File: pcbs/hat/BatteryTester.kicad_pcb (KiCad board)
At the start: 4 copper layers, 162 parts, among them J1 Supply Connector, J2 Battery Connector, J3 Battery Connector, J4 Battery Connector, J5 Battery Connector, J6 Battery Connector, J7 Battery Connector, J8 Battery Connector, J9 Battery Connector, Q1 DMT6009LCT, Q10 AO3414, Q11 DMT6009LCT, Q12 AO3414, Q13 DMT6009LCT, Q14 AO3414, Q15 DMT6009LCT, Q16 AO3414, Q2 AO3414, Q3 DMT6009LCT, Q4 AO3414, Q5 DMT6009LCT, Q6 AO3414, Q7 DMT6009LCT, Q8 AO3414, Q9 DMT6009LCT, U1 INA181A2IDBVR, U10 TP5000_Breakout_Akaddy, U11 INA181A2IDBVR, U12 TP5000_Breakout_Akaddy, U13 INA181A2IDBVR, U14 TP5000_Breakout_Akaddy, U15 INA181A2IDBVR, U16 TP5000_Breakout_Akaddy, U17 NUCLEO-F401RE, U18 ADS7828, U19 ADS7828, U2 TP5000_Breakout_Akaddy, U20 ADS7828, U21 AP2138N-2.5TRG1, U22 LM3480-5.0, U23 SST25VF016B, U3 INA181A2IDBVR, U4 TP5000_Breakout_Akaddy, U5 INA181A2IDBVR, U6 TP5000_Breakout_Akaddy, U7 INA181A2IDBVR, U8 TP5000_Breakout_Akaddy, U9 INA181A2IDBVR

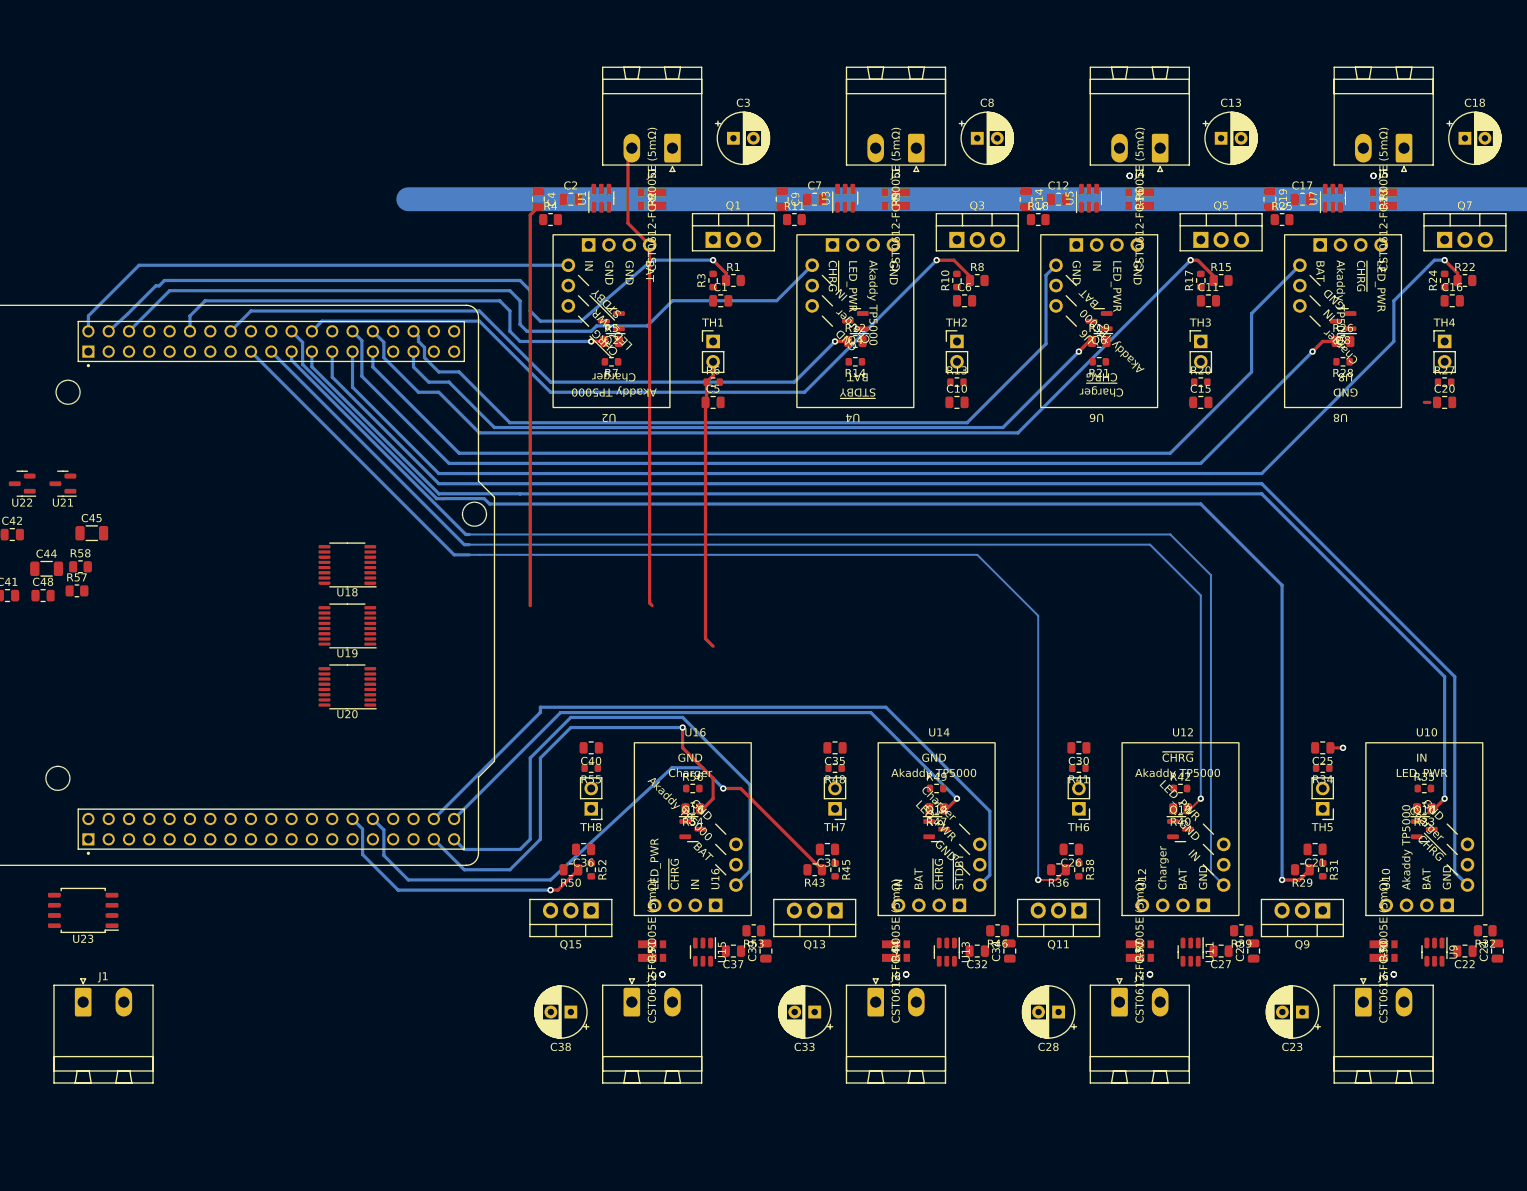
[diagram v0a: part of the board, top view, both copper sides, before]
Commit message: reassign adc's
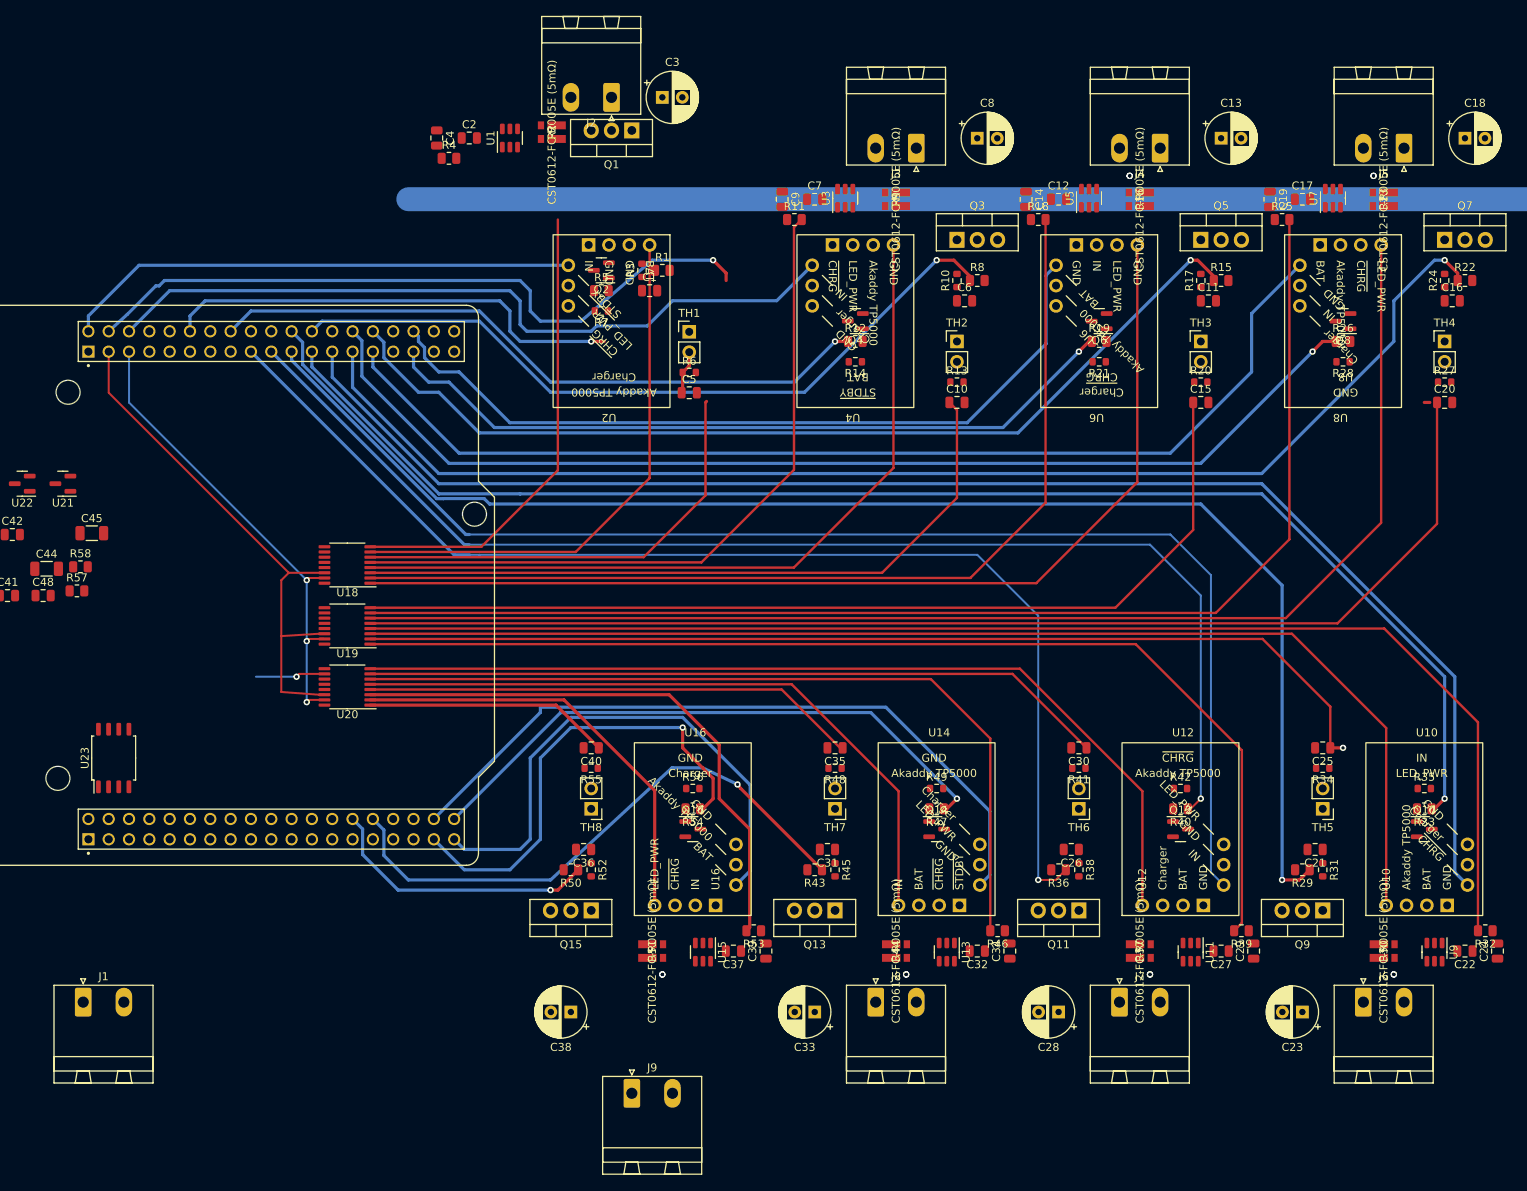
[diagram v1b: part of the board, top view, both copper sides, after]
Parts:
- moved U23 19.4 mm to (336.6, -3.81), turned to 90 degrees
- moved Q1 17.0 mm to (401.3, -82.3), turned to 180 degrees
- moved R2 15.1 mm to (391.3, -82.0)
- moved C4 14.8 mm to (376.9, -81.3)
- moved R4 14.8 mm to (378.5, -78.8)
- moved C2 14.8 mm to (381.0, -81.3)
- moved U1 13.7 mm to (386.1, -81.3)
- moved J9 11.4 mm to (401.3, 38.1)
- moved C3 10.3 mm to (405.1, -86.4)
- moved J2 9.92 mm to (398.8, -86.4)
- moved R3 8.98 mm to (402.6, -64.8)
- moved C1 8.98 mm to (403.5, -62.2)
- moved R1 8.98 mm to (405.1, -64.8)
- moved Q2 6.48 mm to (397.5, -64.8)
- moved R5 6.48 mm to (397.5, -62.2)
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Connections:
- J2 pad 1: /test-battery-1/GNDBAT -> /SENSOR_10
- J2 pad 2: /SENSOR_10 -> /test-battery-1/GNDBAT
- J3 pad 1: /test-battery-2/GNDBAT -> /SENSOR_20
- J3 pad 2: /SENSOR_20 -> /test-battery-2/GNDBAT
- J4 pad 1: /test-battery-3/GNDBAT -> /SENSOR_30
- J4 pad 2: /SENSOR_30 -> /test-battery-3/GNDBAT
- J5 pad 1: /test-battery-4/GNDBAT -> /SENSOR_40
- J5 pad 2: /SENSOR_40 -> /test-battery-4/GNDBAT
- J6 pad 1: /test-battery-5/GNDBAT -> /SENSOR_50
- J6 pad 2: /SENSOR_50 -> /test-battery-5/GNDBAT
- J7 pad 1: /test-battery-6/GNDBAT -> /SENSOR_60
- J7 pad 2: /SENSOR_60 -> /test-battery-6/GNDBAT
- J8 pad 1: /test-battery-7/GNDBAT -> /SENSOR_70
- J8 pad 2: /SENSOR_70 -> /test-battery-7/GNDBAT
- J9 pad 1: /test-battery-8/GNDBAT -> /SENSOR_80
- J9 pad 2: /SENSOR_80 -> /test-battery-8/GNDBAT
- R16 pad 1: /test-battery-3/GNDBAT -> GND
- R16 pad 4: GND -> /test-battery-3/GNDBAT
- R2 pad 1: /test-battery-1/GNDBAT -> GND
- R2 pad 4: GND -> /test-battery-1/GNDBAT
- R23 pad 1: /test-battery-4/GNDBAT -> GND
- R23 pad 4: GND -> /test-battery-4/GNDBAT
- R30 pad 1: /test-battery-5/GNDBAT -> GND
- R30 pad 4: GND -> /test-battery-5/GNDBAT
- R37 pad 1: /test-battery-6/GNDBAT -> GND
- R37 pad 4: GND -> /test-battery-6/GNDBAT
- R44 pad 1: /test-battery-7/GNDBAT -> GND
- R44 pad 4: GND -> /test-battery-7/GNDBAT
- R51 pad 1: /test-battery-8/GNDBAT -> GND
- R51 pad 4: GND -> /test-battery-8/GNDBAT
- R9 pad 1: /test-battery-2/GNDBAT -> GND
- R9 pad 4: GND -> /test-battery-2/GNDBAT
- U18 pad 1: /SENSOR_80 -> /SENSOR_30
- U18 pad 2: /SENSOR_70 -> /SENSOR_31
- U18 pad 3: /SENSOR_60 -> /SENSOR_22
- U18 pad 4: /SENSOR_50 -> /SENSOR_20
- U18 pad 5: /SENSOR_40 -> /SENSOR_21
- U18 pad 6: /SENSOR_30 -> /SENSOR_12
- U18 pad 7: /SENSOR_20 -> /SENSOR_10
- U18 pad 8: /SENSOR_10 -> /SENSOR_11
- U19 pad 1: /SENSOR_81 -> /SENSOR_61
- U19 pad 2: /SENSOR_71 -> /SENSOR_52
- U19 pad 3: /SENSOR_61 -> /SENSOR_50
- U19 pad 5: /SENSOR_41 -> /SENSOR_42
- U19 pad 6: /SENSOR_31 -> /SENSOR_40
- U19 pad 7: /SENSOR_21 -> /SENSOR_41
- U19 pad 8: /SENSOR_11 -> /SENSOR_32
- U20 pad 2: /SENSOR_72 -> /SENSOR_80
- U20 pad 3: /SENSOR_62 -> /SENSOR_81
- U20 pad 4: /SENSOR_52 -> /SENSOR_72
- U20 pad 5: /SENSOR_42 -> /SENSOR_70
- U20 pad 6: /SENSOR_32 -> /SENSOR_71
- U20 pad 7: /SENSOR_22 -> /SENSOR_62
- U20 pad 8: /SENSOR_12 -> /SENSOR_60
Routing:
- net /SENSOR_51: track 0.00 -> 169.4 mm
- net /SENSOR_40: track 0.00 -> 166.0 mm
- net /SENSOR_41: track 0.00 -> 158.7 mm
- net /SENSOR_50: track 0.00 -> 154.0 mm
- net /SENSOR_42: track 0.00 -> 153.7 mm
- net /SENSOR_61: track 0.00 -> 137.4 mm
- net /SENSOR_30: track 0.00 -> 130.8 mm
- net /SENSOR_52: track 1.59 -> 130.3 mm
- net /SENSOR_31: track 0.00 -> 123.7 mm
- net /SENSOR_32: track 0.00 -> 122.8 mm
- net /SENSOR_60: track 0.00 -> 117.1 mm
- net /SENSOR_71: track 0.00 -> 104.6 mm
- net /SENSOR_20: track 0.00 -> 98.4 mm
- net /SENSOR_62: track 0.00 -> 93.4 mm
- net /SENSOR_22: track 0.00 -> 89.5 mm
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
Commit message: pcb layout progress
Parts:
- U17: footprint STS_Boards:ST_Morpho_Connector_64_MountingHoles -> STS_Boards:ST_Morpho_Connector_64
- moved R22 43.4 mm to (463.5, -74.5)
- moved C16 43.4 mm to (463.5, -76.8), turned to 180 degrees
- moved R24 42.3 mm to (463.5, -78.9), turned to 180 degrees
- moved U10 39.5 mm to (457.9, 2.92)
- moved Q7 39.3 mm to (466.1, -82.3), turned to 180 degrees
- moved R23 38.8 mm to (457.9, -83.9)
- moved C24 37.5 mm to (472.6, 13.7), turned to 180 degrees
- moved C25 37.5 mm to (451.9, -16.1)
- moved R34 37.5 mm to (451.9, -13.6)
- moved TH5 37.3 mm to (451.9, -7.87)
- moved R33 37.1 mm to (464.0, -4.70)
- moved Q10 36.8 mm to (463.9, -0.25)
- moved U7 36.7 mm to (453.6, -83.8)
- moved R35 36.6 mm to (463.9, -2.92)
- moved C17 36.2 mm to (450.4, -83.8), turned to 90 degrees
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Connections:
- U18 pad 2: /SENSOR_31 -> /SENSOR_22
- U18 pad 3: /SENSOR_22 -> /SENSOR_31
- U18 pad 5: /SENSOR_21 -> /SENSOR_12
- U18 pad 6: /SENSOR_12 -> /SENSOR_21
- U19 pad 1: /SENSOR_61 -> /SENSOR_52
- U19 pad 2: /SENSOR_52 -> /SENSOR_61
- U19 pad 7: /SENSOR_41 -> /SENSOR_32
- U19 pad 8: /SENSOR_32 -> /SENSOR_41
- U20 pad 3: /SENSOR_81 -> /SENSOR_72
- U20 pad 4: /SENSOR_72 -> /SENSOR_81
- U20 pad 6: /SENSOR_71 -> /SENSOR_62
- U20 pad 7: /SENSOR_62 -> /SENSOR_71
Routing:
- net +5V: track 0.00 -> 236.5 mm, vias 0 -> 17
- net Vref_I_SENS: track 0.00 -> 192.1 mm, vias 12 -> 8
- net /SENSOR_53: track 185.7 -> 0.00 mm
- net /SIGNAL_50: track 176.9 -> 0.00 mm, vias 1 -> 0
- net (no net): track 173.4 -> 0.00 mm
- net /SIGNAL_51: track 179.4 -> 12.8 mm
- net /SENSOR_63: track 166.5 -> 0.00 mm
- net /SIGNAL_60: track 156.4 -> 0.00 mm, vias 1 -> 0
- net /SIGNAL_41: track 162.7 -> 12.8 mm
- net GND: track 0.00 -> 149.8 mm, vias 0 -> 40
- net /SIGNAL_40: track 138.7 -> 0.00 mm, vias 1 -> 0
- net /SIGNAL_61: track 149.1 -> 12.8 mm
- net /SENSOR_43: track 136.3 -> 0.00 mm
- net /SIGNAL_31: track 121.8 -> 12.8 mm
- net /SENSOR_33: track 99.3 -> 0.00 mm
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- added copper zone on B.Cu, net /SENSOR_10
- added copper zone on F.Cu, net /SENSOR_10
- added copper zone on B.Cu, net /SENSOR_20
- added copper zone on F.Cu, net /SENSOR_20
- added copper zone on B.Cu, net /SENSOR_30
- added copper zone on F.Cu, net /SENSOR_30
- added copper zone on B.Cu, net /SENSOR_40
- added copper zone on F.Cu, net /SENSOR_40
- added copper zone on B.Cu, net /SENSOR_50
- added copper zone on F.Cu, net /SENSOR_50
- added copper zone on B.Cu, net /SENSOR_60
- added copper zone on F.Cu, net /SENSOR_60
- added copper zone on B.Cu, net /SENSOR_70
- added copper zone on F.Cu, net /SENSOR_70
- added copper zone on B.Cu, net /SENSOR_80
- added copper zone on F.Cu, net /SENSOR_80
- added copper zone on B.Cu, net /test-battery-1/GNDBAT
- added copper zone on F.Cu, net /test-battery-1/GNDBAT
- added copper zone on B.Cu, net /test-battery-2/GNDBAT
- added copper zone on F.Cu, net /test-battery-2/GNDBAT
- added copper zone on B.Cu, net /test-battery-3/GNDBAT
- added copper zone on F.Cu, net /test-battery-3/GNDBAT
- added copper zone on B.Cu, net /test-battery-4/GNDBAT
- added copper zone on F.Cu, net /test-battery-4/GNDBAT
- added copper zone on B.Cu, net /test-battery-5/GNDBAT
- added copper zone on F.Cu, net /test-battery-5/GNDBAT
- added copper zone on B.Cu, net /test-battery-6/GNDBAT
- added copper zone on F.Cu, net /test-battery-6/GNDBAT
- added copper zone on B.Cu, net /test-battery-7/GNDBAT
- added copper zone on F.Cu, net /test-battery-7/GNDBAT
- added copper zone on B.Cu, net /test-battery-8/GNDBAT
- added copper zone on F.Cu, net /test-battery-8/GNDBAT
- added copper zone on B.Cu, net GND
- added copper zone on F.Cu, net GND
- added copper zone on In1.Cu, net GND
- added copper zone on In2.Cu, net GND
- added copper zone on B.Cu, net VCC
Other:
- board outline added: 165.1 x 138.7 mm

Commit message: wip
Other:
- board size 165.1 x 138.7 mm -> 165.1 x 132.1 mm
